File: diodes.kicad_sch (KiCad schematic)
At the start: 32 parts

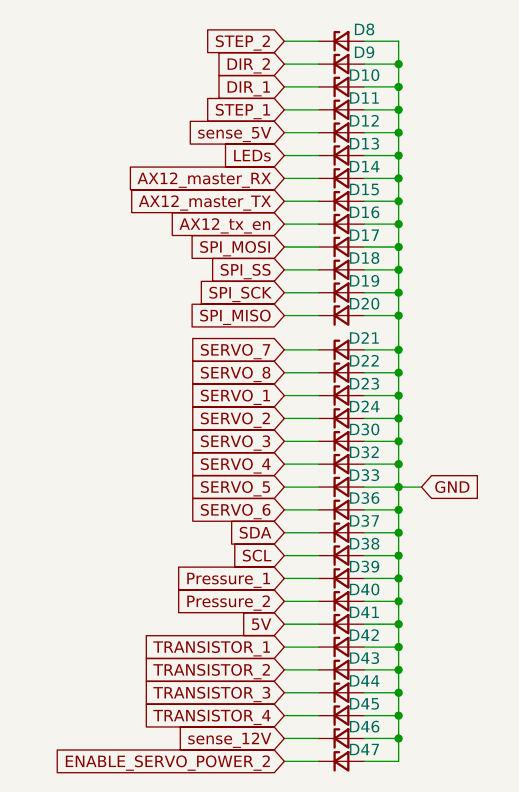
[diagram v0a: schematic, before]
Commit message: remove intra-board zeners
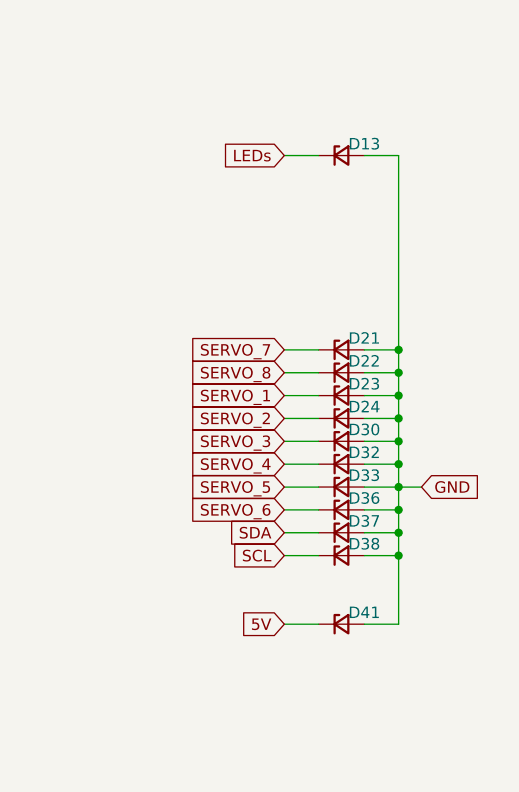
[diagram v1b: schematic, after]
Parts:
- removed D10, D11, D12, D14, D15, D16, D17, D18, D19, D20, D39, D40, D42, D43, D44, D45, D46, D47, D8, D9: D_Zener_Small, Diode_SMD:D_SOD-123, symbol Device:D_Zener_Small

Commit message: Add BOM
Add LCSC reference and correct few footprint acording bom
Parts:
- D13, D21, D22, D23, D24, D30, D32, D33, D36, D37, D38, D41: LCSC# (none) -> C908230
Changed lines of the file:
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@@
+			)
+		)
+		(property "LCSC#" "C908230"
+			(at 118.11 96.52 0)
+			(effects
+				(font
+					(size 1.27 1.27)
+				)
+				(hide yes)
 			)
 		)
@@
 			)
 		)
+		(property "LCSC#" "C908230"
+			(at 118.11 114.3 0)
+			(effects
+				(font
+					(size 1.27 1.27)
+				)
+				(hide yes)
+			)
+		)
 		(pin "1"
 		)
@@
 			)
 		)
+		(property "LCSC#" "C908230"
+			(at 118.11 109.22 0)
+			(effects
+				(font
+					(size 1.27 1.27)
+				)
+				(hide yes)
+			)
+		)
 		(pin "1"
 		)
@@
 			)
 		)
+		(property "LCSC#" "C908230"
+			(at 118.11 119.38 0)
+			(effects
+				(font
+					(size 1.27 1.27)
+				)
+				(hide yes)
+			)
+		)
 		(pin "1"
 		)
@@
 			)
 		)
+		(property "LCSC#" "C908230"
+			(at 118.11 127 0)
+			(effects
+				(font
+					(size 1.27 1.27)
+				)
+				(hide yes)
+			)
+		)
 		(pin "1"
 		)
@@
 			)
 		)
+		(property "LCSC#" "C908230"
+			(at 118.11 111.76 0)
+			(effects
+				(font
+					(size 1.27 1.27)
+				)
+				(hide yes)
+			)
+		)
 		(pin "1"
 		)
@@
 			)
 		)
+		(property "LCSC#" "C908230"
+			(at 118.11 106.68 0)
+			(effects
+				(font
+					(size 1.27 1.27)
+				)
+				(hide yes)
+			)
+		)
 		(pin "1"
 		)
@@
 			)
 		)
+		(property "LCSC#" "C908230"
+			(at 118.11 116.84 0)
+			(effects
+				(font
+					(size 1.27 1.27)
+				)
+				(hide yes)
+			)
+		)
 		(pin "1"
 		)
@@
 			)
 		)
+		(property "LCSC#" "C908230"
+			(at 118.11 74.93 0)
+			(effects
+				(font
+					(size 1.27 1.27)
+				)
+				(hide yes)
+			)
+		)
 		(pin "1"
 		)
@@
 			)
 		)
+		(property "LCSC#" "C908230"
+			(at 118.11 101.6 0)
+			(effects
+				(font
+					(size 1.27 1.27)
+				)
+				(hide yes)
+			)
+		)
 		(pin "1"
 		)
@@
 			)
 		)
+		(property "LCSC#" "C908230"
+			(at 118.11 104.14 0)
+			(effects
+				(font
+					(size 1.27 1.27)
+				)
+				(hide yes)
+			)
+		)
 		(pin "1"
 		)
@@
 			(at 118.11 99.06 0)
 			(effects
+				(font
+					(size 1.27 1.27)
+				)
+				(hide yes)
+			)
+		)
+		(property "LCSC#" "C908230"
+			(at 118.11 99.06 0)
+			(effects

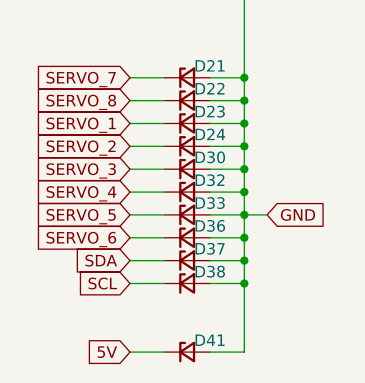
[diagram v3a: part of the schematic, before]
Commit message: fix warnings + add big capa on 6V DCDC input
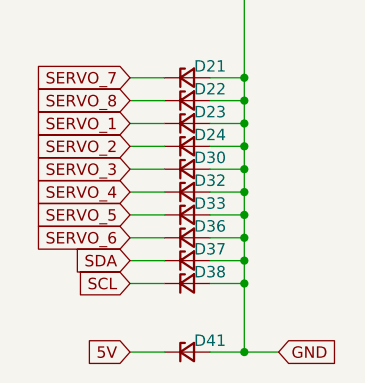
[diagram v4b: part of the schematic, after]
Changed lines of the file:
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@@
 	(paper "A4")
 	(junction
+		(at 124.46 127)
+		(diameter 0)
+		(color 0 0 0 0)
+	)
+	(junction
 		(at 124.46 116.84)
 		(diameter 0)
@@
 	(wire
 		(pts
+			(xy 124.46 116.84) (xy 124.46 114.3)
+		)
+		(stroke
+			(width 0)
+			(type default)
+		)
+	)
+	(wire
+		(pts
 			(xy 120.65 96.52) (xy 124.46 96.52)
 		)
@@
 	(wire
 		(pts
-			(xy 124.46 111.76) (xy 124.46 114.3)
-		)
-		(stroke
-			(width 0)
-			(type default)
-		)
-	)
-	(wire
-		(pts
 			(xy 111.76 111.76) (xy 115.57 111.76)
 		)
@@
 	(wire
 		(pts
-			(xy 124.46 114.3) (xy 124.46 116.84)
-		)
-		(stroke
-			(width 0)
-			(type default)
-		)
-	)
-	(wire
-		(pts
 			(xy 111.76 101.6) (xy 115.57 101.6)
 		)
@@
 	(wire
 		(pts
-			(xy 124.46 111.76) (xy 127 111.76)
+			(xy 124.46 127) (xy 128.27 127)
 		)
 		(stroke
@@
 	(wire
 		(pts
+			(xy 124.46 119.38) (xy 124.46 116.84)
+		)
+		(stroke
+			(width 0)
+			(type default)
+		)
+	)
+	(wire
+		(pts
 			(xy 120.65 74.93) (xy 124.46 74.93)
 		)
@@
 	(wire
 		(pts
-			(xy 124.46 116.84) (xy 124.46 119.38)
-		)
-		(stroke
-			(width 0)
-			(type default)
-		)
-	)
-	(wire
-		(pts
 			(xy 111.76 96.52) (xy 115.57 96.52)
 		)
@@
 		)
 	)
+	(wire
+		(pts
+			(xy 124.46 114.3) (xy 124.46 111.76)
+		)
+		(stroke
+			(width 0)
+			(type default)
+		)
+	)
 	(global_label "SERVO_8"
 		(shape input)
@@
 	(global_label "GND"
 		(shape input)
-		(at 127 111.76 0)
+		(at 128.27 127 0)
 		(fields_autoplaced yes)
 		(effects
@@
 		)
 		(property "Intersheetrefs" "${INTERSHEET_REFS}"
-			(at 133.2836 111.6806 0)
-			(effects
-				(font
+			(at 134.5536 126.9206 0)
+			(effects
+				(font
